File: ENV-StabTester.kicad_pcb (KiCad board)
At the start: 2 copper layers, 140 x 48 mm, 14 parts, among them SW2 SW_Push, SW5 SW_Push, SW6 SW_Push, SW7 SW_Push, SW8 SW_Push

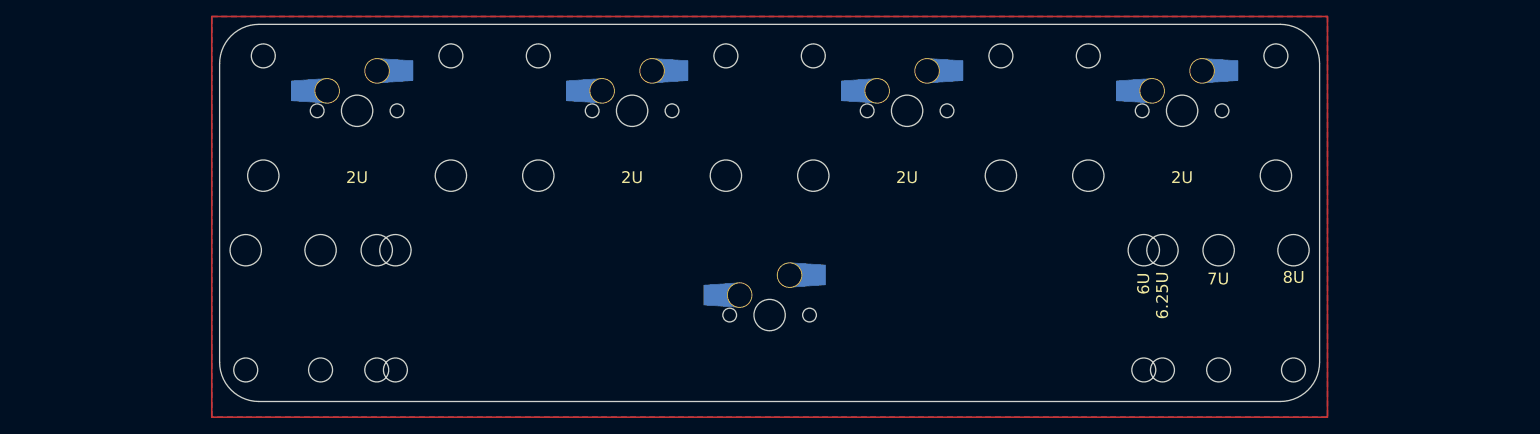
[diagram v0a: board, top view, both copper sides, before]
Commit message: fixed incorrect spacing on top row
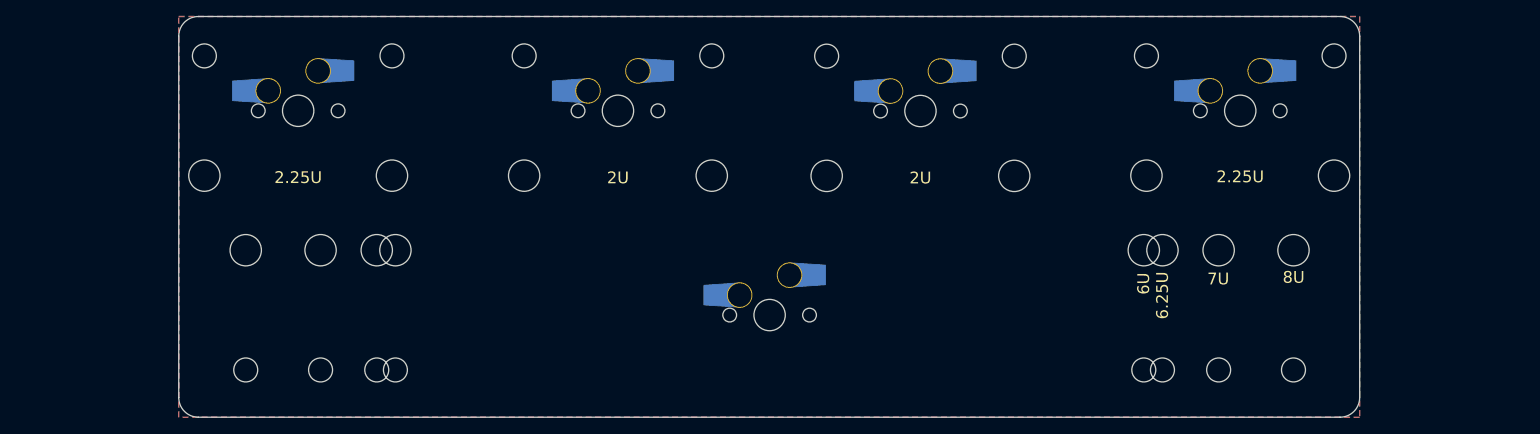
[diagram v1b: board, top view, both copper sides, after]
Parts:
- moved SW2 7.50 mm to (41.0, 43.0)
- moved stb3 7.50 mm to (41.0, 43.0)
- moved SW7 7.40 mm to (160.9, 43.0)
- moved stb4 7.40 mm to (160.9, 43.0)
- moved SW8 1.80 mm to (81.7, 43.0)
- moved stb1 1.80 mm to (81.7, 43.0)
- moved SW6 1.70 mm to (120.2, 43.0)
- moved stb2 1.70 mm to (120.2, 43.0)
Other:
- board size 140 x 48 mm -> 150.3 x 51 mm
- board text added: "2.25U"
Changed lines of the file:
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@@
       (drillshape 0)
       (scaleselection 1)
-      (outputdirectory "")
+      (outputdirectory "Gerbers/")
     )
   )
@@
   (net 10 "unconnected-(SW8-Pad2)")
   (footprint "Mounting_Keyboard_Stabilizer:Stabilizer_Cherry_MX_2u" (layer "F.Cu")
-    (at 83.5 43)
+    (at 81.7 43)
     (descr "Cherry MX key stabilizer 2u 2.25u 2.5u 2.75u")
     (tags "Cherry MX key stabilizer 2u 2.25u 2.5u 2.75u")
@@
   )
   (footprint "Switch_Keyboard_Cherry_MX:MXOnly-1U-Hotswap-Modified" (layer "F.Cu")
-    (at 153.5 43)
+    (at 160.9 43)
     (property "Sheetfile" "ENV-StabTester.kicad_sch")
     (property "Sheetname" "")
@@
   )
   (footprint "Mounting_Keyboard_Stabilizer:Stabilizer_Cherry_MX_2u" (layer "F.Cu")
-    (at 48.5 43)
+    (at 41 43)
     (descr "Cherry MX key stabilizer 2u 2.25u 2.5u 2.75u")
     (tags "Cherry MX key stabilizer 2u 2.25u 2.5u 2.75u")
@@
   )
   (footprint "Mounting_Keyboard_Stabilizer:Stabilizer_Cherry_MX_2u" (layer "F.Cu")
-    (at 118.5 43)
+    (at 120.2 43.03005)
     (descr "Cherry MX key stabilizer 2u 2.25u 2.5u 2.75u")
     (tags "Cherry MX key stabilizer 2u 2.25u 2.5u 2.75u")
@@
   )
   (footprint "Switch_Keyboard_Cherry_MX:MXOnly-1U-Hotswap-Modified" (layer "F.Cu")
-    (at 48.5 43)
+    (at 41 43)
     (property "Sheetfile" "ENV-StabTester.kicad_sch")
     (property "Sheetname" "")
@@
   )
   (footprint "Switch_Keyboard_Cherry_MX:MXOnly-1U-Hotswap-Modified" (layer "F.Cu")
-    (at 118.5 43)
+    (at 120.2 43.03005)
     (property "Sheetfile" "ENV-StabTester.kicad_sch")
     (property "Sheetname" "")
@@
   )
   (footprint "Switch_Keyboard_Cherry_MX:MXOnly-1U-Hotswap-Modified" (layer "F.Cu")
-    (at 83.5 43)
+    (at 81.7 43)
     (property "Sheetfile" "ENV-StabTester.kicad_sch")
     (property "Sheetname" "")
@@
   )
   (footprint "Mounting_Keyboard_Stabilizer:Stabilizer_Cherry_MX_2u" (layer "F.Cu")
-    (at 153.5 43)
+    (at 160.9 43)
     (descr "Cherry MX key stabilizer 2u 2.25u 2.5u 2.75u")
     (tags "Cherry MX key stabilizer 2u 2.25u 2.5u 2.75u")
@@
       ) (layer "B.SilkS") (width 0) (fill solid))
   )
-  (gr_rect (start 30 31) (end 172 82) (layer "F.Cu") (width 0.2) (fill none))
-  (gr_arc (start 31 37) (mid 32.464466 33.464466) (end 36 32) (layer "Edge.Cuts") (width 0.1))
-  (gr_arc (start 171 75) (mid 169.535534 78.535534) (end 166 80) (layer "Edge.Cuts") (width 0.1))
-  (gr_line (start 166 80) (end 36 80) (layer "Edge.Cuts") (width 0.1))
-  (gr_line (start 171 37) (end 171 75) (layer "Edge.Cuts") (width 0.1))
-  (gr_arc (start 36 80) (mid 32.464466 78.535534) (end 31 75) (layer "Edge.Cuts") (width 0.1))
-  (gr_line (start 36 32) (end 166 32) (layer "Edge.Cuts") (width 0.1))
-  (gr_line (start 31 75) (end 31 37) (layer "Edge.Cuts") (width 0.1))
-  (gr_arc (start 166 32) (mid 169.535534 33.464466) (end 171 37) (layer "Edge.Cuts") (width 0.1))
+  (gr_line (start 176.1 33.5) (end 176.1 79.5) (layer "Edge.Cuts") (width 0.1))
+  (gr_arc (start 176.1 79.5) (mid 175.367767 81.267767) (end 173.6 82) (layer "Edge.Cuts") (width 0.1))
+  (gr_line (start 25.8 79.5) (end 25.8 33.5) (layer "Edge.Cuts") (width 0.1))
+  (gr_line (start 28.3 31) (end 173.6 31) (layer "Edge.Cuts") (width 0.1))
+  (gr_line (start 173.6 82) (end 28.3 82) (layer "Edge.Cuts") (width 0.1))
+  (gr_arc (start 173.6 31) (mid 175.367767 31.732233) (end 176.1 33.5) (layer "Edge.Cuts") (width 0.1))
+  (gr_arc (start 28.3 82) (mid 26.532233 81.267767) (end 25.8 79.5) (layer "Edge.Cuts") (width 0.1))
+  (gr_arc (start 25.8 33.5) (mid 26.532233 31.732233) (end 28.3 31) (layer "Edge.Cuts") (width 0.1))
   (gr_text "http://github.com/envious-data" (at 101 78.7) (layer "B.SilkS")
     (effects (font (size 0.8 0.8) (thickness 0.15)) (justify mirror))
@@
     (effects (font (size 1.5 1.5) (thickness 0.3)))
   )
-  (gr_text "2U" (at 83.5 51.5) (layer "F.SilkS")
+  (gr_text "2U" (at 81.7 51.531794) (layer "F.SilkS")
     (effects (font (size 1.5 1.5) (thickness 0.3)))
   )
@@
     (effects (font (size 1.5 1.5) (thickness 0.3)))
   )
-  (gr_text "2U" (at 48.5 51.5) (layer "F.SilkS")
+  (gr_text "2.25U" (at 41 51.5) (layer "F.SilkS")
     (effects (font (size 1.5 1.5) (thickness 0.3)))
   )
-  (gr_text "2U" (at 118.5 51.5) (layer "F.SilkS")
+  (gr_text "2U" (at 120.2 51.550297) (layer "F.SilkS")
     (effects (font (size 1.5 1.5) (thickness 0.3)))
   )
@@
     (effects (font (size 1.5 1.5) (thickness 0.3)))
   )
-  (gr_text "2U" (at 153.5 51.5) (layer "F.SilkS")
+  (gr_text "2.25U" (at 160.9 51.4) (layer "F.SilkS")
     (effects (font (size 1.5 1.5) (thickness 0.3)))
   )
@@
     (polygon
       (pts
-        (xy 30 31)
-        (xy 172 31)
-        (xy 172 82)
-        (xy 30 82)
+        (xy 25.8 31)
+        (xy 176.1 31)
+        (xy 176.1 82)
+        (xy 25.8 82)
       )
     )

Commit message: updated again to fit 2.75U and 2.25U instead of 2.25+2U
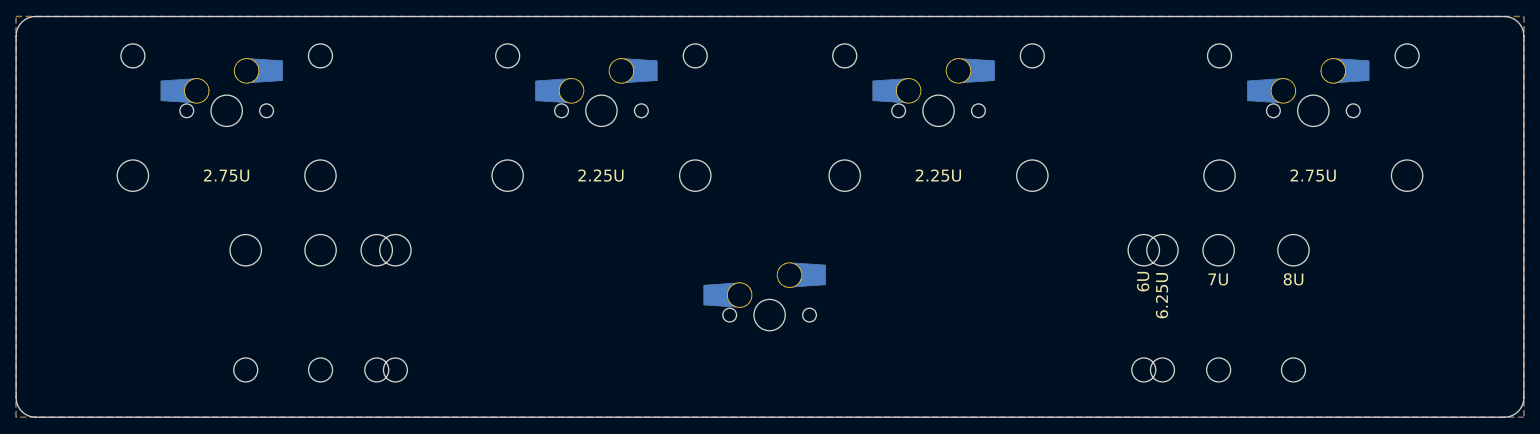
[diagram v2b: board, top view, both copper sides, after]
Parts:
- moved SW7 9.30 mm to (170.2, 43.0)
- moved stb4 9.30 mm to (170.2, 43.0)
- moved SW2 9.10 mm to (31.9, 43.0)
- moved stb3 9.10 mm to (31.9, 43.0)
- moved SW6 2.30 mm to (122.5, 43.0)
- moved stb2 2.30 mm to (122.5, 43.0)
- moved SW8 2.10 mm to (79.6, 43.0)
- moved stb1 2.10 mm to (79.6, 43.0)
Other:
- board size 150.3 x 51 mm -> 191.9 x 51 mm
- board text added: "2.75U"
- board text removed: "2U"
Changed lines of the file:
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@@
   (net 10 "unconnected-(SW8-Pad2)")
   (footprint "Mounting_Keyboard_Stabilizer:Stabilizer_Cherry_MX_2u" (layer "F.Cu")
-    (at 81.7 43)
+    (at 79.6 43)
     (descr "Cherry MX key stabilizer 2u 2.25u 2.5u 2.75u")
     (tags "Cherry MX key stabilizer 2u 2.25u 2.5u 2.75u")
@@
   )
   (footprint "Switch_Keyboard_Cherry_MX:MXOnly-1U-Hotswap-Modified" (layer "F.Cu")
-    (at 160.9 43)
+    (at 170.2 43)
     (property "Sheetfile" "ENV-StabTester.kicad_sch")
     (property "Sheetname" "")
@@
   )
   (footprint "Mounting_Keyboard_Stabilizer:Stabilizer_Cherry_MX_2u" (layer "F.Cu")
-    (at 41 43)
+    (at 31.9 43)
     (descr "Cherry MX key stabilizer 2u 2.25u 2.5u 2.75u")
     (tags "Cherry MX key stabilizer 2u 2.25u 2.5u 2.75u")
@@
   )
   (footprint "Mounting_Keyboard_Stabilizer:Stabilizer_Cherry_MX_2u" (layer "F.Cu")
-    (at 120.2 43.03005)
+    (at 122.5 43)
     (descr "Cherry MX key stabilizer 2u 2.25u 2.5u 2.75u")
     (tags "Cherry MX key stabilizer 2u 2.25u 2.5u 2.75u")
@@
   )
   (footprint "Switch_Keyboard_Cherry_MX:MXOnly-1U-Hotswap-Modified" (layer "F.Cu")
-    (at 41 43)
+    (at 31.9 43)
     (property "Sheetfile" "ENV-StabTester.kicad_sch")
     (property "Sheetname" "")
@@
   )
   (footprint "Switch_Keyboard_Cherry_MX:MXOnly-1U-Hotswap-Modified" (layer "F.Cu")
-    (at 120.2 43.03005)
+    (at 122.5 43)
     (property "Sheetfile" "ENV-StabTester.kicad_sch")
     (property "Sheetname" "")
@@
   )
   (footprint "Switch_Keyboard_Cherry_MX:MXOnly-1U-Hotswap-Modified" (layer "F.Cu")
-    (at 81.7 43)
+    (at 79.6 43)
     (property "Sheetfile" "ENV-StabTester.kicad_sch")
     (property "Sheetname" "")
@@
   )
   (footprint "Mounting_Keyboard_Stabilizer:Stabilizer_Cherry_MX_2u" (layer "F.Cu")
-    (at 160.9 43)
+    (at 170.2 43)
     (descr "Cherry MX key stabilizer 2u 2.25u 2.5u 2.75u")
     (tags "Cherry MX key stabilizer 2u 2.25u 2.5u 2.75u")
@@
       ) (layer "B.SilkS") (width 0) (fill solid))
   )
-  (gr_line (start 176.1 33.5) (end 176.1 79.5) (layer "Edge.Cuts") (width 0.1))
-  (gr_arc (start 176.1 79.5) (mid 175.367767 81.267767) (end 173.6 82) (layer "Edge.Cuts") (width 0.1))
-  (gr_line (start 25.8 79.5) (end 25.8 33.5) (layer "Edge.Cuts") (width 0.1))
-  (gr_line (start 28.3 31) (end 173.6 31) (layer "Edge.Cuts") (width 0.1))
-  (gr_line (start 173.6 82) (end 28.3 82) (layer "Edge.Cuts") (width 0.1))
-  (gr_arc (start 173.6 31) (mid 175.367767 31.732233) (end 176.1 33.5) (layer "Edge.Cuts") (width 0.1))
-  (gr_arc (start 28.3 82) (mid 26.532233 81.267767) (end 25.8 79.5) (layer "Edge.Cuts") (width 0.1))
-  (gr_arc (start 25.8 33.5) (mid 26.532233 31.732233) (end 28.3 31) (layer "Edge.Cuts") (width 0.1))
+  (gr_line (start 197 33.5) (end 197 79.5) (layer "Edge.Cuts") (width 0.1))
+  (gr_arc (start 197 79.5) (mid 196.267767 81.267767) (end 194.5 82) (layer "Edge.Cuts") (width 0.1))
+  (gr_line (start 5.1 79.5) (end 5.1 33.5) (layer "Edge.Cuts") (width 0.1))
+  (gr_line (start 7.6 31) (end 194.5 31) (layer "Edge.Cuts") (width 0.1))
+  (gr_line (start 194.5 82) (end 7.6 82) (layer "Edge.Cuts") (width 0.1))
+  (gr_arc (start 194.5 31) (mid 196.267767 31.732233) (end 197 33.5) (layer "Edge.Cuts") (width 0.1))
+  (gr_arc (start 7.6 82) (mid 5.832233 81.267767) (end 5.1 79.5) (layer "Edge.Cuts") (width 0.1))
+  (gr_arc (start 5.1 33.5) (mid 5.832233 31.732233) (end 7.6 31) (layer "Edge.Cuts") (width 0.1))
   (gr_text "http://github.com/envious-data" (at 101 78.7) (layer "B.SilkS")
     (effects (font (size 0.8 0.8) (thickness 0.15)) (justify mirror))
   )
-  (gr_text "6U" (at 148.6 65 90) (layer "F.SilkS")
+  (gr_text "6U" (at 148.6 64.729999 90) (layer "F.SilkS")
     (effects (font (size 1.5 1.5) (thickness 0.3)))
   )
-  (gr_text "7U" (at 158.1 64.4) (layer "F.SilkS")
+  (gr_text "7U" (at 158.1 64.512499) (layer "F.SilkS")
     (effects (font (size 1.5 1.5) (thickness 0.3)))
   )
-  (gr_text "2U" (at 81.7 51.531794) (layer "F.SilkS")
+  (gr_text "2.75U" (at 31.9 51.3) (layer "F.SilkS")
     (effects (font (size 1.5 1.5) (thickness 0.3)))
   )
-  (gr_text "6.25U" (at 151 66.5 90) (layer "F.SilkS")
+  (gr_text "6.25U" (at 151 66.515714 90) (layer "F.SilkS")
     (effects (font (size 1.5 1.5) (thickness 0.3)))
   )
-  (gr_text "2.25U" (at 41 51.5) (layer "F.SilkS")
+  (gr_text "2.25U" (at 79.55 51.3) (layer "F.SilkS")
     (effects (font (size 1.5 1.5) (thickness 0.3)))
   )
-  (gr_text "2U" (at 120.2 51.550297) (layer "F.SilkS")
+  (gr_text "2.75U" (at 170.2 51.3) (layer "F.SilkS")
     (effects (font (size 1.5 1.5) (thickness 0.3)))
   )
-  (gr_text "8U" (at 167.7 64.2) (layer "F.SilkS")
+  (gr_text "8U" (at 167.7 64.512499) (layer "F.SilkS")
     (effects (font (size 1.5 1.5) (thickness 0.3)))
   )
-  (gr_text "2.25U" (at 160.9 51.4) (layer "F.SilkS")
+  (gr_text "2.25U" (at 122.5 51.3) (layer "F.SilkS")
     (effects (font (size 1.5 1.5) (thickness 0.3)))
   )
@@
     (polygon
       (pts
-        (xy 25.8 31)
-        (xy 176.1 31)
-        (xy 176.1 82)
-        (xy 25.8 82)
+        (xy 5.1 31)
+        (xy 197 31)
+        (xy 197 82)
+        (xy 5.1 82)
       )
     )
